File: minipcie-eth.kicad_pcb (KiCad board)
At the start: 2 copper layers, 142.7 x 47 mm, 40 parts, among them J1 UART2, J2 GPIO, J3 Micro_SD, J4 SD, U1 VoCore_v2, U2 si3404, U3 ap2112, U4 MPCIE-Socket, X1 SI-52003-F

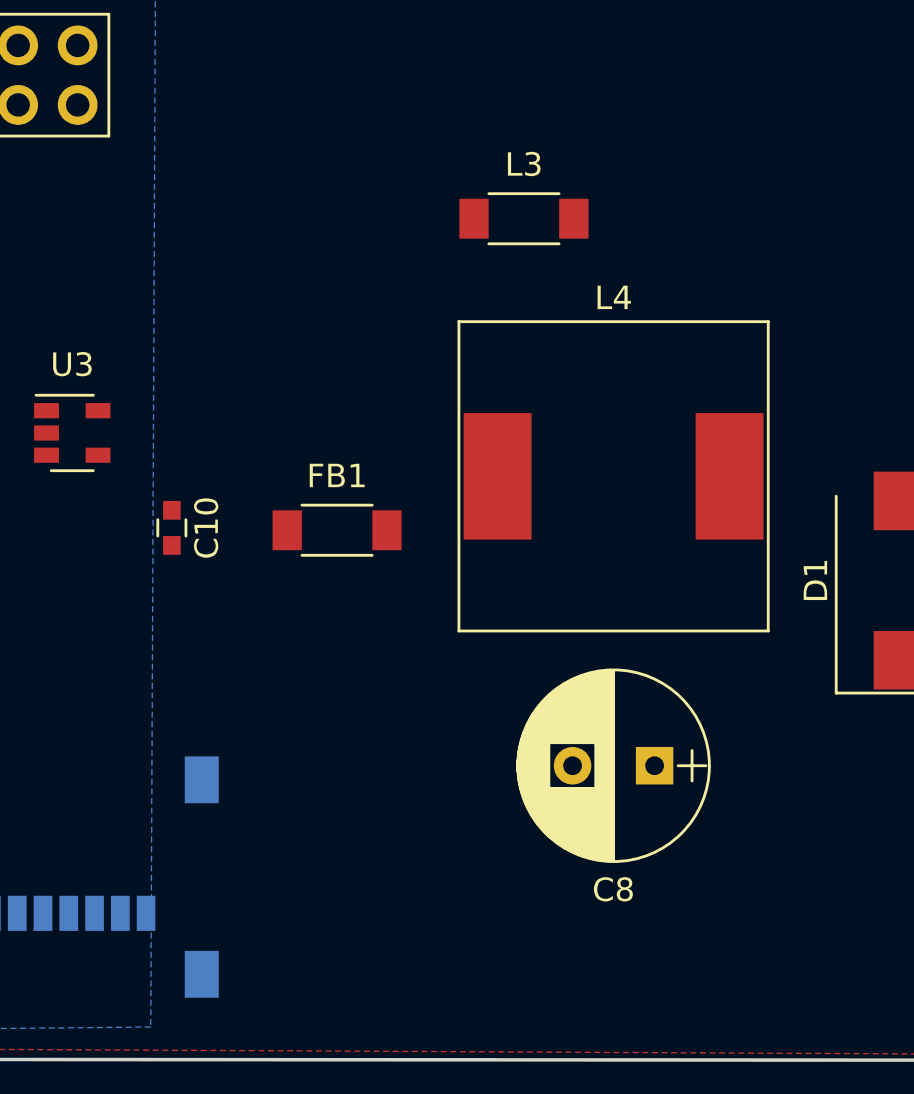
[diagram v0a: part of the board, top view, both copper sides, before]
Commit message: Correct main coil (from coilcraft) footprint
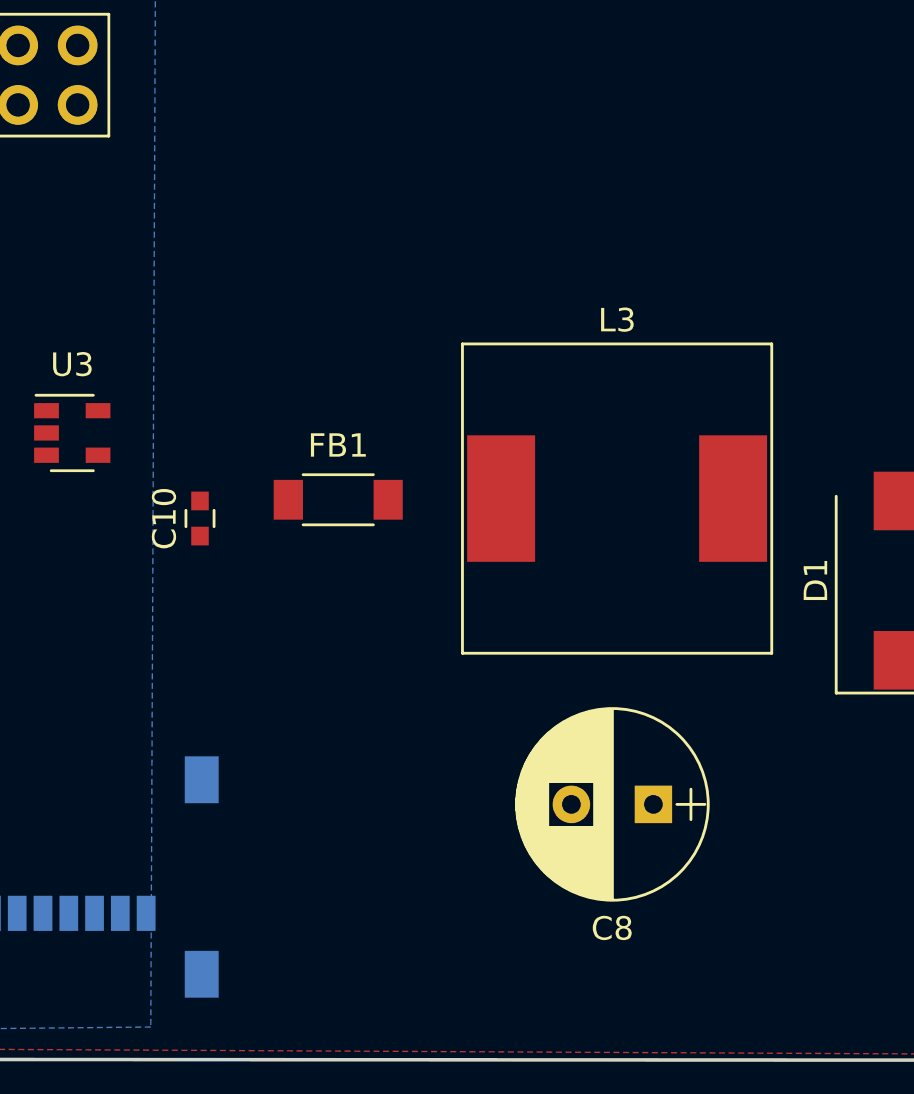
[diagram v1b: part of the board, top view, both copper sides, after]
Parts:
- removed L4: 30Ohm, KiCad/Inductors_SMD.pretty:L_Neosid_SM-NE127
- L3: footprint KiCad/Inductors_SMD.pretty:L_1806 -> KiCad/Inductors_SMD.pretty:L_Neosid_SM-NE127
- moved L3 12.6 mm to (183.2, 67.8)
- moved C8 1.65 mm to (184.7, 80.9)
- moved FB1 1.30 mm to (171.2, 67.9)
- moved C10 1.26 mm to (165.3, 68.7), turned to 90 degrees
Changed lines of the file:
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@@
   (tracks 0)
   (zones 0)
-  (modules 40)
+  (modules 39)
   (nets 114)
 )
@@
   (tracks 0)
   (zones 0)
-  (modules 40)
+  (modules 39)
   (nets 114)
 )
@@
   )
   (module KiCad/Capacitors_SMD.pretty:C_0603 (layer F.Cu)
-    (at 164.15 69.1 270)
+    (at 165.35 68.7 90)
     (descr "Capacitor SMD 0603, reflow soldering, AVX (see smccp.pdf)")
     (tags "capacitor 0603")
     (attr smd)
-    (fp_text reference C10 (at 0 -1.5 270) (layer F.SilkS)
-      (effects (font (size 1 1) (thickness 0.15)))
-    )
-    (fp_text value 22uF/6.3V (at 0 1.5 270) (layer F.Fab)
+    (fp_text reference C10 (at 0 -1.5 90) (layer F.SilkS)
+      (effects (font (size 1 1) (thickness 0.15)))
+    )
+    (fp_text value 22uF/6.3V (at 0 1.5 90) (layer F.Fab)
       (effects (font (size 1 1) (thickness 0.15)))
     )
@@
     (fp_line (start 0.8 0.4) (end -0.8 0.4) (layer F.Fab) (width 0.1))
     (fp_line (start -0.8 0.4) (end -0.8 -0.4) (layer F.Fab) (width 0.1))
-    (fp_text user %R (at 0 0 270) (layer F.Fab)
+    (fp_text user %R (at 0 0 90) (layer F.Fab)
       (effects (font (size 0.3 0.3) (thickness 0.075)))
     )
-    (pad 2 smd rect (at 0.75 0 270) (size 0.8 0.75) (layers F.Cu F.Paste F.Mask)
-      (net 10 GND))
-    (pad 1 smd rect (at -0.75 0 270) (size 0.8 0.75) (layers F.Cu F.Paste F.Mask)
+    (pad 2 smd rect (at 0.75 0 90) (size 0.8 0.75) (layers F.Cu F.Paste F.Mask)
+      (net 10 GND))
+    (pad 1 smd rect (at -0.75 0 90) (size 0.8 0.75) (layers F.Cu F.Paste F.Mask)
       (net 3 +5V))
     (model Capacitors_SMD.3dshapes/C_0603.wrl
@@
       (rotate (xyz 0 0 0))
     )
-  )
-  (module KiCad/Inductors_SMD.pretty:L_Neosid_SM-NE127 (layer F.Cu)
-    (at 183 66.9)
-    (descr "Neosid, Inductor, SM-NE127, Festinduktivitaet, SMD,")
-    (tags "Neosid Inductor SM-NE127 Festinduktivitaet SMD")
-    (attr smd)
-    (fp_text reference L4 (at 0 -7.6) (layer F.SilkS)
-      (effects (font (size 1 1) (thickness 0.15)))
-    )
-    (fp_text value 30Ohm (at 0 7.7) (layer F.Fab)
-      (effects (font (size 1 1) (thickness 0.15)))
-    )
-    (fp_circle (center 0 0) (end 5 0) (layer F.Fab) (width 0.1))
-    (fp_line (start 6.65 6.65) (end -6.65 6.65) (layer F.CrtYd) (width 0.05))
-    (fp_line (start 6.65 6.65) (end 6.65 -6.65) (layer F.CrtYd) (width 0.05))
-    (fp_line (start -6.65 -6.65) (end -6.65 6.65) (layer F.CrtYd) (width 0.05))
-    (fp_line (start -6.65 -6.65) (end 6.65 -6.65) (layer F.CrtYd) (width 0.05))
-    (fp_line (start -6.4 6.4) (end -6.4 -6.4) (layer F.Fab) (width 0.1))
-    (fp_line (start 6.4 6.4) (end -6.4 6.4) (layer F.Fab) (width 0.1))
-    (fp_line (start 6.4 -6.4) (end 6.4 6.4) (layer F.Fab) (width 0.1))
-    (fp_line (start -6.4 -6.4) (end 6.4 -6.4) (layer F.Fab) (width 0.1))
-    (fp_line (start 6.6 6.6) (end -6.6 6.6) (layer F.SilkS) (width 0.12))
-    (fp_line (start 6.6 -6.6) (end 6.6 6.6) (layer F.SilkS) (width 0.12))
-    (fp_line (start -6.6 -6.6) (end 6.6 -6.6) (layer F.SilkS) (width 0.12))
-    (fp_line (start -6.6 6.6) (end -6.6 -6.6) (layer F.SilkS) (width 0.12))
-    (pad 1 smd rect (at -4.95 0) (size 2.9 5.4) (layers F.Cu F.Paste F.Mask)
-      (net 10 GND))
-    (pad 2 smd rect (at 4.95 0) (size 2.9 5.4) (layers F.Cu F.Paste F.Mask)
-      (net 9 "Net-(C8-Pad2)"))
   )
   (module KiCad/Resistors_SMD.pretty:R_0603 (layer F.Cu)
@@
   )
   (module KiCad/Capacitors_ThroughHole.pretty:CP_Radial_D8.0mm_P3.50mm (layer F.Cu)
-    (at 184.75 79.25 180)
+    (at 184.7 80.9 180)
     (descr "CP, Radial series, Radial, pin pitch=3.50mm, , diameter=8mm, Electrolytic Capacitor")
     (tags "CP Radial series Radial pin pitch 3.50mm  diameter 8mm Electrolytic Capacitor")
@@
   )
   (module KiCad/Inductors_SMD.pretty:L_1806 (layer F.Cu)
-    (at 171.2 69.2)
+    (at 171.25 67.9)
     (descr "Ferrite bead SMD 1806, reflow soldering, see Murata BLM41P")
     (tags "ferrite bead 1806")
@@
     (pad 1 smd rect (at -2.13 0) (size 1.25 1.7) (layers F.Cu F.Paste F.Mask)
       (net 10 GND))
-    (model Inductors_SMD.3dshapes\L_1806.wrl
-      (at (xyz 0 0 0))
-      (scale (xyz 1 1 1))
-      (rotate (xyz 0 0 0))
-    )
-  )
-  (module KiCad/Inductors_SMD.pretty:L_1806 (layer F.Cu)
-    (at 179.175001 55.9075)
-    (descr "Ferrite bead SMD 1806, reflow soldering, see Murata BLM41P")
-    (tags "ferrite bead 1806")
-    (attr smd)
-    (fp_text reference L3 (at 0 -2.3) (layer F.SilkS)
-      (effects (font (size 1 1) (thickness 0.15)))
-    )
-    (fp_text value 33uH (at 0 2.3) (layer F.Fab)
-      (effects (font (size 1 1) (thickness 0.15)))
-    )
-    (fp_text user %R (at 0 0) (layer F.Fab)
-      (effects (font (size 1 1) (thickness 0.15)))
-    )
-    (fp_line (start -2.25 0.8) (end -2.25 -0.8) (layer F.Fab) (width 0.1))
-    (fp_line (start 2.25 0.8) (end -2.25 0.8) (layer F.Fab) (width 0.1))
-    (fp_line (start 2.25 -0.8) (end 2.25 0.8) (layer F.Fab) (width 0.1))
-    (fp_line (start -2.25 -0.8) (end 2.25 -0.8) (layer F.Fab) (width 0.1))
-    (fp_line (start -3 -1.2) (end 3 -1.2) (layer F.CrtYd) (width 0.05))
-    (fp_line (start -3 1.2) (end 3 1.2) (layer F.CrtYd) (width 0.05))
-    (fp_line (start -3 -1.2) (end -3 1.2) (layer F.CrtYd) (width 0.05))
-    (fp_line (start 3 -1.2) (end 3 1.2) (layer F.CrtYd) (width 0.05))
-    (fp_line (start 1.5 1.07) (end -1.5 1.07) (layer F.SilkS) (width 0.12))
-    (fp_line (start -1.5 -1.07) (end 1.5 -1.07) (layer F.SilkS) (width 0.12))
-    (pad 1 smd rect (at -2.13 0) (size 1.25 1.7) (layers F.Cu F.Paste F.Mask)
-      (net 9 "Net-(C8-Pad2)"))
-    (pad 2 smd rect (at 2.13 0) (size 1.25 1.7) (layers F.Cu F.Paste F.Mask)
-      (net 112 "Net-(D1-Pad2)"))
     (model Inductors_SMD.3dshapes\L_1806.wrl
       (at (xyz 0 0 0))
@@
     )
   )
+  (module KiCad/Inductors_SMD.pretty:L_Neosid_SM-NE127 (layer F.Cu)
+    (at 183.15 67.85)
+    (descr "Neosid, Inductor, SM-NE127, Festinduktivitaet, SMD,")
+    (tags "Neosid Inductor SM-NE127 Festinduktivitaet SMD")
+    (attr smd)
+    (fp_text reference L3 (at 0 -7.6) (layer F.SilkS)
+      (effects (font (size 1 1) (thickness 0.15)))
+    )
+    (fp_text value 33uH (at 0 7.7) (layer F.Fab)
+      (effects (font (size 1 1) (thickness 0.15)))
+    )
+    (fp_line (start -6.6 6.6) (end -6.6 -6.6) (layer F.SilkS) (width 0.12))
+    (fp_line (start -6.6 -6.6) (end 6.6 -6.6) (layer F.SilkS) (width 0.12))
+    (fp_line (start 6.6 -6.6) (end 6.6 6.6) (layer F.SilkS) (width 0.12))
+    (fp_line (start 6.6 6.6) (end -6.6 6.6) (layer F.SilkS) (width 0.12))
+    (fp_line (start -6.4 -6.4) (end 6.4 -6.4) (layer F.Fab) (width 0.1))
+    (fp_line (start 6.4 -6.4) (end 6.4 6.4) (layer F.Fab) (width 0.1))
+    (fp_line (start 6.4 6.4) (end -6.4 6.4) (layer F.Fab) (width 0.1))
+    (fp_line (start -6.4 6.4) (end -6.4 -6.4) (layer F.Fab) (width 0.1))
+    (fp_line (start -6.65 -6.65) (end 6.65 -6.65) (layer F.CrtYd) (width 0.05))
+    (fp_line (start -6.65 -6.65) (end -6.65 6.65) (layer F.CrtYd) (width 0.05))
+    (fp_line (start 6.65 6.65) (end 6.65 -6.65) (layer F.CrtYd) (width 0.05))
+    (fp_line (start 6.65 6.65) (end -6.65 6.65) (layer F.CrtYd) (width 0.05))
+    (fp_circle (center 0 0) (end 5 0) (layer F.Fab) (width 0.1))
+    (pad 2 smd rect (at 4.95 0) (size 2.9 5.4) (layers F.Cu F.Paste F.Mask)
+      (net 112 "Net-(D1-Pad2)"))
+    (pad 1 smd rect (at -4.95 0) (size 2.9 5.4) (layers F.Cu F.Paste F.Mask)
+      (net 9 "Net-(C8-Pad2)"))
+  )
   (gr_line (start 105 44.8) (end 247.05 45.2) (layer Edge.Cuts) (width 0.15))
